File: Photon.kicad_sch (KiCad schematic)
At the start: 62 parts, among them J1 USB_C_Receptacle_USB2.0_14P, SW1 TS-1088-AR02016, U1 ATtiny13A-S, U2 RT8059GJ5, U3 BQ24072RGTR, U4 BCR421UW6-7, U5 BCR421UW6-7, U6 DW01A, U7 FS8205A, U8 TP4056

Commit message: added usb detection circuit and battery protection
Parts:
- removed C3, C4, C7: 4.7uF, Capacitor_SMD:C_0603_1608Metric, symbol Device:C
- removed D1, D2: SZYY0603R1, LED_SMD:LED_0603_1608Metric, symbol Device:LED
- removed R11, R7: 1.18K, Resistor_SMD:R_0603_1608Metric, symbol Device:R
- removed R21, R6, R8: 1K, Resistor_SMD:R_0603_1608Metric, symbol Device:R
- removed R5: 0R, Resistor_SMD:R_0603_1608Metric, symbol Device:R
- removed TP8: BuckEN, TestPoint:TestPoint_Pad_D1.0mm, symbol Connector:TestPoint
- removed TP9: BAT+, TestPoint:TestPoint_Pad_D1.0mm, symbol Connector:TestPoint
- removed U3: BQ24072RGTR, Photon:QFN-16_EP_3.8x3.8_Pitch0.5mm, symbol Photon:BQ24074RGTR
- added D8: D_Schottky, Diode_SMD:D_SOD-323F, symbol Device:D_Schottky
- added Q1: IRLML6402, Package_TO_SOT_SMD:SOT-23, symbol Transistor_FET:IRLML6402
- added R22: 100K, Resistor_SMD:R_0603_1608Metric, symbol Device:R
- added R23: 10K, Resistor_SMD:R_0603_1608Metric, symbol Device:R
- added TP10: BuckEN, TestPoint:TestPoint_Pad_D1.0mm, symbol Connector:TestPoint
- C10: Rating (none) -> XR5
- D3: Supplier https://jlcpcb.com/partdetail/YongyuPhotoelectric-SZYY0603R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 -> https://www.lcsc.com/datasheet/C19712529.pdf
- D6: Supplier https://jlcpcb.com/partdetail/YongyuPhotoelectric-SZYY0603R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 -> https://www.lcsc.com/datasheet/C19712529.pdfSZYY0603R1/C197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
- D7: Supplier https://jlcpcb.com/partdetail/YongyuPhotoelectric-SZYY0603R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 -> https://www.lcsc.com/datasheet/C19712529.pdf; Vf (none) -> 2V
- R10: value 100K -> 62K; Tolerance (none) -> 1%
- R13, R15, R3: value 10K -> 100K
- R18, R19: Tolerance (none) -> 1%
- R20: value 1K -> 2K
- R4: value 10K -> 0R
- R9: value 500K -> 280K; Tolerance (none) -> 1%
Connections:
- net 5V: now also R23.1
- net GND: now also R22.2; no longer R4.1
- net PACK+: now also Q1.3 (D); no longer U2.1 (EN)
- net LED_PWR: now reaches D6.2 (A)
- net LED_PWR: now also D7.2 (A), R20.2
- net STAT2: now reaches D7.1 (K), U8.6 (STAT2)
- net Iset: now reaches R19.1, U8.2 (ISET)
- net STAT1: now reaches D6.1 (K), U8.7 (STAT1)
- net VM: now reaches R18.2, U6.2 (VM)
- net BAT_SAF_OUT: now reaches C8.1, U6.6 (GND), U7.1 (S1)
- net BAT_SAF_OUT: now also D8.1 (K); no longer BT1.2 (-)
- net OC: now reaches U6.3 (OC), U7.4 (G2)
- net OD: now reaches U6.1 (OD), U7.6 (G1)
- net DW01A_VCC: now reaches C8.2, R17.2, U6.5 (VCC)
- net LED_A: now reaches D3.2 (A), R12.2
- net 3V6 renamed +3V3
- net TS renamed PMOS_OUT
- net PMOS_OUT: now also Q1.2 (S)
- new net: BT1.2 (-), D8.2 (A)
- new net BUCK_EN: R4.1, TP10.1, U2.1 (EN)
- new net PMOS_Gate: Q1.1 (G), R22.1, R23.2
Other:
- note added: "18650 Battery Vout=3.7V to 4.2V"
- note added: "Buck_FB = 0.6V Vo = 0.6 * (1+R1/R2) R2 = 60K to 300K"
- note added: "If usb present = disable buck"
- note added: "PACK Output = 3.39V to 3.89V"
- note added: "Vf = 0.31"
- note added: "Vf = 2V"
- note removed: "18650 Battery Vout=3.7-4.2V"
- note removed: "Vo = 0.6 * (1+R1/R2) R2 = 60K to 300K"
- moved on the sheet: C1, C2, C5, C6, D3, D4, D5, D6, D7, L1, R10, R12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

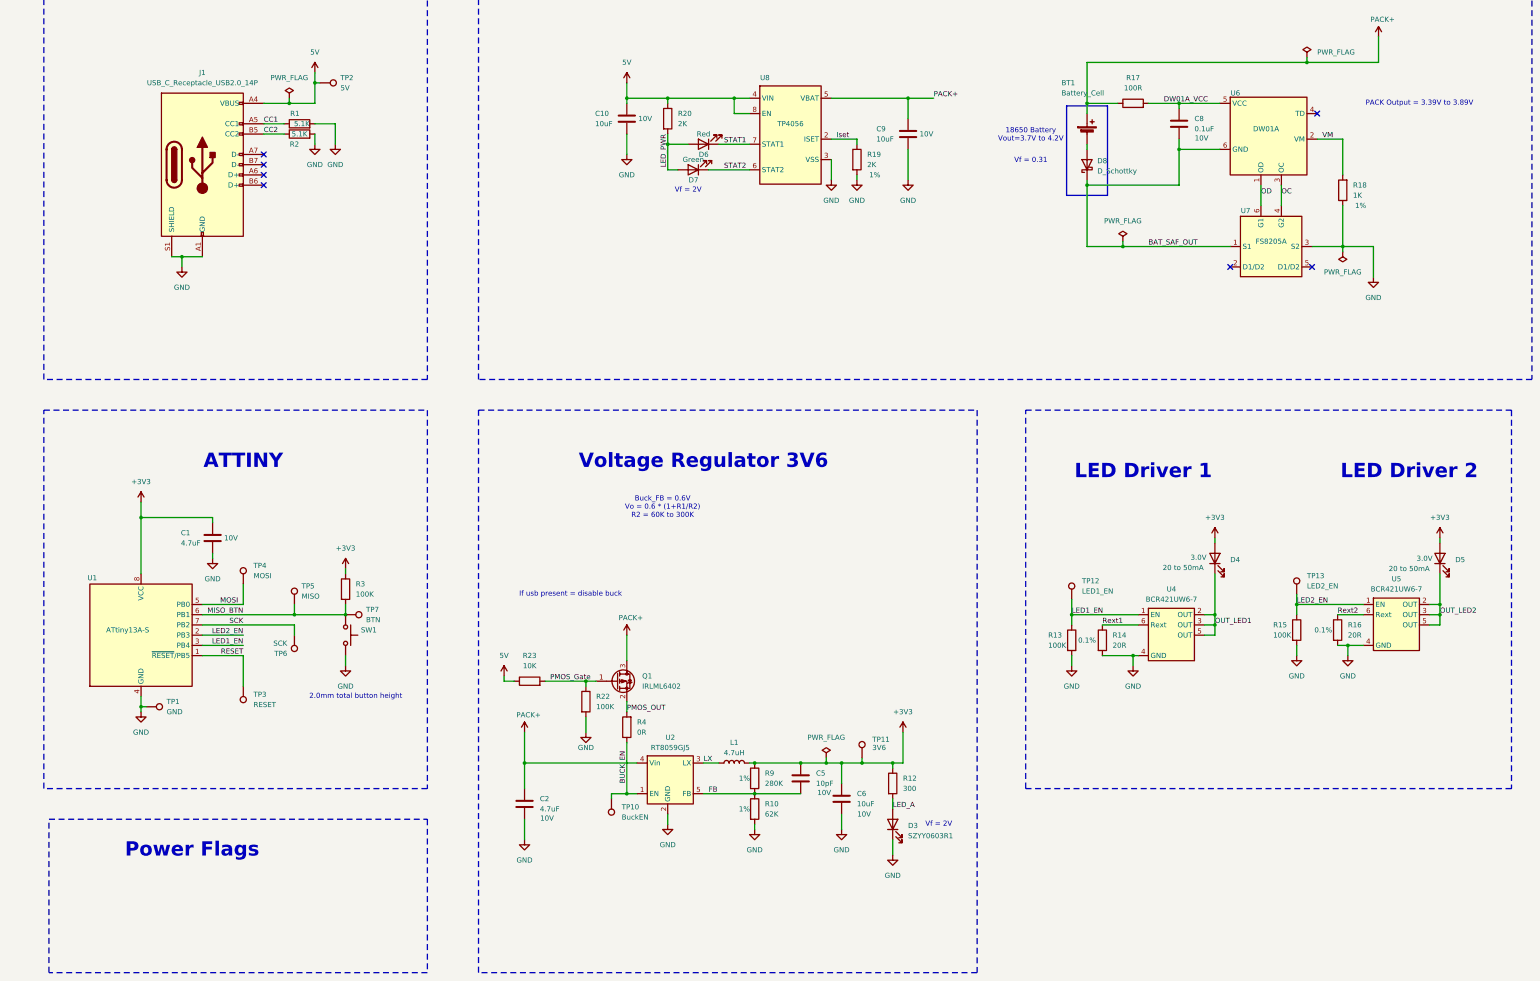
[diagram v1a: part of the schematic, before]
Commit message: PCB layout complete
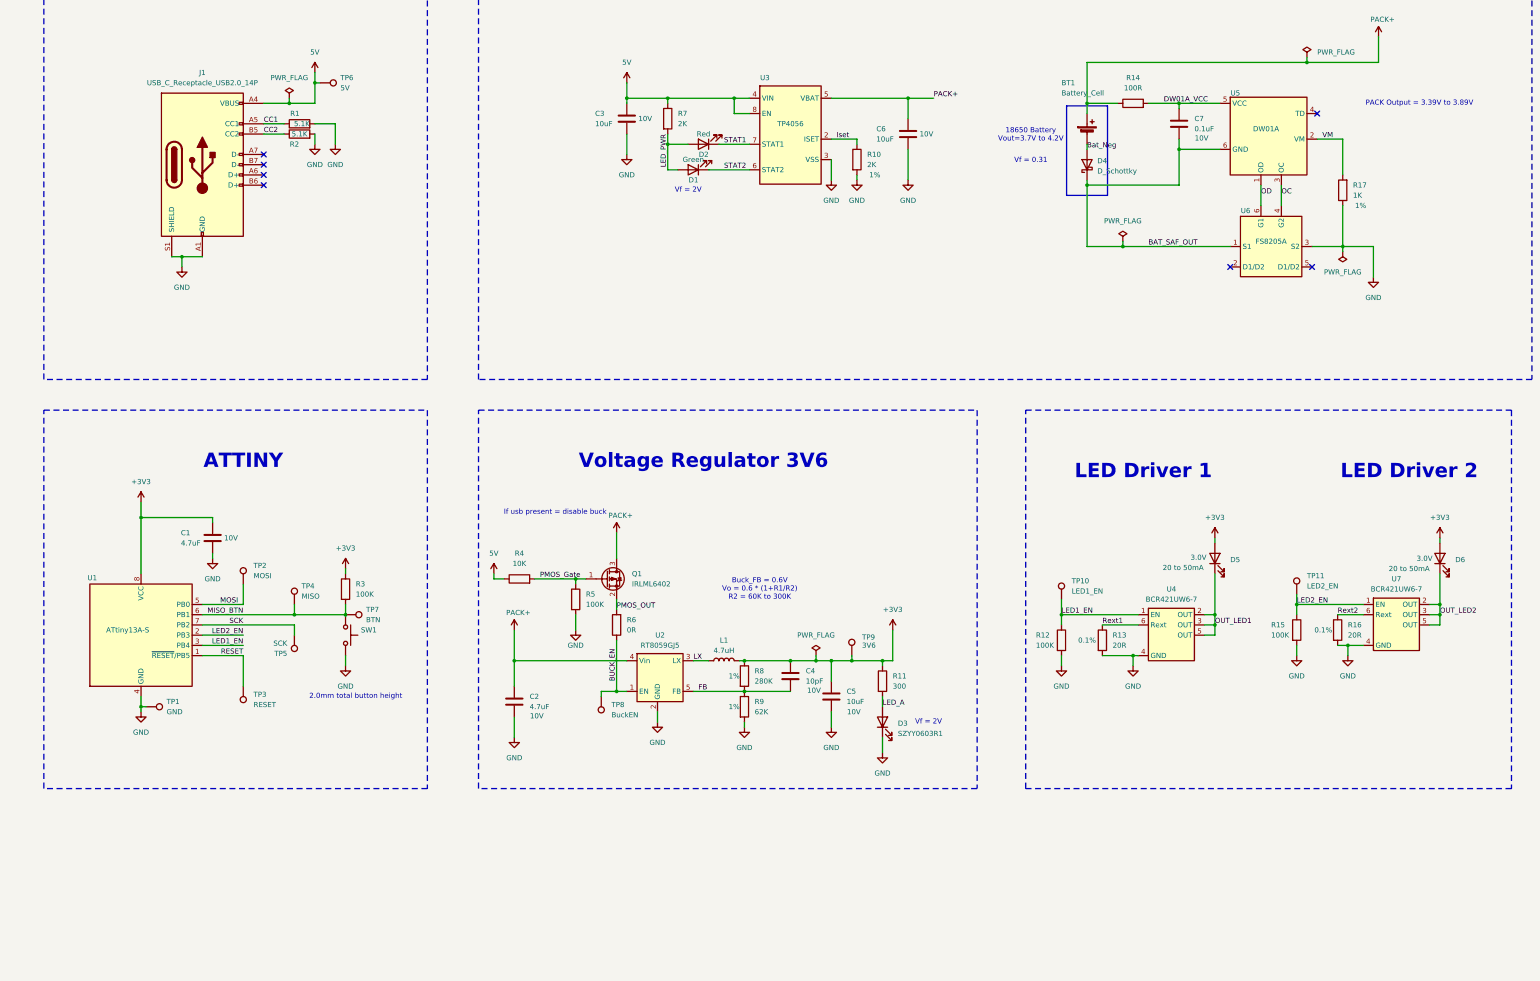
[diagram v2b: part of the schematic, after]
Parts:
- D4: renamed from D8; footprint Diode_SMD:D_SOD-323F -> Diode_SMD:D_SOD-323_HandSoldering
- U2: footprint Package_TO_SOT_SMD:SOT-23-5 -> Package_TO_SOT_SMD:SOT-23-5_HandSoldering
- U4: footprint Package_TO_SOT_SMD:SOT-23-6 -> Package_TO_SOT_SMD:SOT-23-6_Handsoldering
- U5: renamed from U6; footprint Package_TO_SOT_SMD:SOT-23-6 -> Package_TO_SOT_SMD:SOT-23-6_Handsoldering
- U6: renamed from U7; footprint Package_TO_SOT_SMD:SOT-23-6 -> Package_TO_SOT_SMD:SOT-23-6_Handsoldering
- U7: renamed from U5; footprint Package_TO_SOT_SMD:SOT-23-6 -> Package_TO_SOT_SMD:SOT-23-6_Handsoldering
- renumbered C10 to C3, C5 to C4, C6 to C5, C9 to C6, C8 to C7, D7 to D1, D6 to D2, D4 to D5, D5 to D6, R19 to R10, R12 to R11, R13 to R12, R14 to R13, R17 to R14, R18 to R17, R23 to R4, R22 to R5, R4 to R6, R20 to R7, R9 to R8, R10 to R9, TP12 to TP10, TP13 to TP11, TP4 to TP2, TP5 to TP4, TP6 to TP5, TP2 to TP6, TP10 to TP8, TP11 to TP9, U8 to U3
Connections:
- net Bat_Neg: now reaches BT1.2 (-), D4.2 (A)
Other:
- note removed: "Power Flags"
- moved on the sheet: C2, C4, C5, D3, L1, Q1, R11, R12, R4, R5, R6, R8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

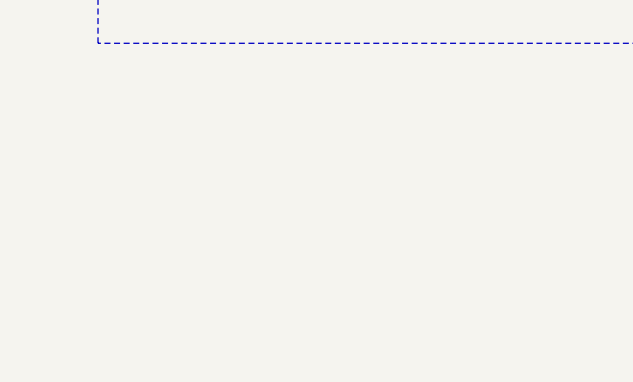
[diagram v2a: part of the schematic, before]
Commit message: added fiducials and gerbers. - Ordered
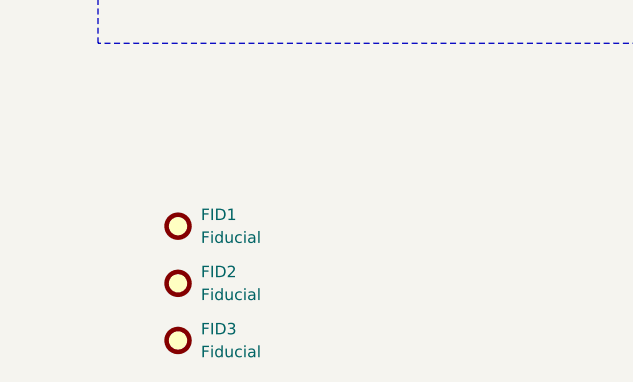
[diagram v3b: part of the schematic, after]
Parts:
- added FID1, FID2, FID3: Fiducial, Fiducial:Fiducial_0.5mm_Mask1.5mm, symbol Mechanical:Fiducial
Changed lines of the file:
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@@
 	)
 	(symbol
+		(lib_id "Mechanical:Fiducial")
+		(at 30.48 262.89 0)
+		(unit 1)
+		(exclude_from_sim no)
+		(in_bom no)
+		(on_board yes)
+		(dnp no)
+		(fields_autoplaced yes)
+		(property "Reference" "FID2"
+			(at 33.02 261.6199 0)
+			(effects
+				(font
+					(size 1.27 1.27)
+				)
+				(justify left)
+			)
+		)
+		(property "Value" "Fiducial"
+			(at 33.02 264.1599 0)
+			(effects
+				(font
+					(size 1.27 1.27)
+				)
+				(justify left)
+			)
+		)
+		(property "Footprint" "Fiducial:Fiducial_0.5mm_Mask1.5mm"
+			(at 30.48 262.89 0)
+			(effects
+				(font
+					(size 1.27 1.27)
+				)
+				(hide yes)
+			)
+		)
+		(property "Datasheet" "~"
+			(at 30.48 262.89 0)
+			(effects
+				(font
+					(size 1.27 1.27)
+				)
+				(hide yes)
+			)
+		)
+		(property "Description" "Fiducial Marker"
+			(at 30.48 262.89 0)
+			(effects
+				(font
+					(size 1.27 1.27)
+				)
+				(hide yes)
+			)
+		)
+		(instances
+			(project "Photon"
+				(path "/bca5ecdc-285a-4b7d-b583-3c5baee62e6e"
+					(reference "FID2")
+					(unit 1)
+				)
+			)
+		)
+	)
+	(symbol
 		(lib_id "power:GND")
 		(at 345.44 203.2 0)
@@
 	)
 	(symbol
+		(lib_id "Mechanical:Fiducial")
+		(at 30.48 256.54 0)
+		(unit 1)
+		(exclude_from_sim no)
+		(in_bom no)
+		(on_board yes)
+		(dnp no)
+		(fields_autoplaced yes)
+		(property "Reference" "FID1"
+			(at 33.02 255.2699 0)
+			(effects
+				(font
+					(size 1.27 1.27)
+				)
+				(justify left)
+			)
+		)
+		(property "Value" "Fiducial"
+			(at 33.02 257.8099 0)
+			(effects
+				(font
+					(size 1.27 1.27)
+				)
+				(justify left)
+			)
+		)
+		(property "Footprint" "Fiducial:Fiducial_0.5mm_Mask1.5mm"
+			(at 30.48 256.54 0)
+			(effects
+				(font
+					(size 1.27 1.27)
+				)
+				(hide yes)
+			)
+		)
+		(property "Datasheet" "~"
+			(at 30.48 256.54 0)
+			(effects
+				(font
+					(size 1.27 1.27)
+				)
+				(hide yes)
+			)
+		)
+		(property "Description" "Fiducial Marker"
+			(at 30.48 256.54 0)
+			(effects
+				(font
+					(size 1.27 1.27)
+				)
+				(hide yes)
+			)
+		)
+		(instances
+			(project ""
+				(path "/bca5ecdc-285a-4b7d-b583-3c5baee62e6e"
+					(reference "FID1")
+					(unit 1)
+				)
+			)
+		)
+	)
+	(symbol
 		(lib_id "Device:R")
 		(at 223.52 80.01 0)
@@
 					(unit 1)
 				)
+			)
+		)
+	)
+	(symbol
+		(lib_id "Mechanical:Fiducial")
+		(at 30.48 269.24 0)
+		(unit 1)
+		(exclude_from_sim no)
+		(in_bom no)
+		(on_board yes)
+		(dnp no)
+		(fields_autoplaced yes)
+		(property "Reference" "FID3"
+			(at 33.02 267.9699 0)
+			(effects
+				(font
+					(size 1.27 1.27)
+				)
+				(justify left)
+			)
+		)
+		(property "Value" "Fiducial"
+			(at 33.02 270.5099 0)
+			(effects
+				(font
+					(size 1.27 1.27)
+				)
+				(justify left)
+			)
+		)
+		(property "Footprint" "Fiducial:Fiducial_0.5mm_Mask1.5mm"
+			(at 30.48 269.24 0)
+			(effects
+				(font
+					(size 1.27 1.27)
+				)
+				(hide yes)
+			)
+		)
+		(property "Datasheet" "~"
+			(at 30.48 269.24 0)
+			(effects
+				(font
+					(size 1.27 1.27)
+				)
+				(hide yes)
+			)
+		)
+		(property "Description" "Fiducial Marker"
+			(at 30.48 269.24 0)
+			(effects
+				(font
+					(size 1.27 1.27)
+				)
+				(hide yes)
+			)
+		)
+		(instances
+			(project "Photon"
+				(path "/bca5ecdc-285a-4b7d-b583-3c5baee62e6e"
+					(reference "FID3")
+					(unit 1)
+				)

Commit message: updated gerbers
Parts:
- removed D4: D_Schottky, Diode_SMD:D_SOD-323_HandSoldering, symbol Device:D_Schottky
- added Q2: IRLML6402, Package_TO_SOT_SMD:SOT-23, symbol Transistor_FET:IRLML6402
- added R18: 10K, Resistor_SMD:R_0603_1608Metric, symbol Device:R
- added R19: 100K, Resistor_SMD:R_0603_1608Metric, symbol Device:R
- L1: value 4.7uH -> 2.2uH
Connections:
- net Bat_Neg is gone; now on net BAT_SAF_OUT: BT1.2 (-)
- net +3V3: now also R18.1
- net BAT_SAF_OUT: now also R19.2
- net PACK+: now also Q2.2 (S); no longer BT1.1 (+), R14.1
- net RESET: now also R18.2
- new net: Q2.1 (G), R19.1
- new net Bat+: BT1.1 (+), Q2.3 (D), R14.1
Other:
- note added: "PACK Output = 3.7V to 4.2V"
- note added: "Rds = 0.065R"
- note removed: "PACK Output = 3.39V to 3.89V"
- note removed: "Vf = 0.31"
- moved on the sheet: R3, SW1, TP3, TP4, TP5, TP7

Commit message: finished v3 of pcb
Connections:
- net BAT_DSBL: now reaches Q2.1 (G), R19.1
- net BAT_SAF_OUT renamed Bat-
- net PMOS_Gate renamed USB_DSBL
- net PMOS_OUT renamed PMOS_EN_OUT
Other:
- moved on the sheet: BT1
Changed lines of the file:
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@@
 	)
 	(rectangle
-		(start 275.59 66.675)
-		(end 285.75 88.9)
+		(start 275.59 64.77)
+		(end 285.75 80.01)
 		(stroke
 			(width 0)
@@
 	)
 	(junction
-		(at 280.67 86.36)
-		(diameter 0)
-		(color 0 0 0 0)
-	)
-	(junction
 		(at 345.44 200.66)
 		(diameter 0)
@@
 	)
 	(junction
+		(at 280.67 77.47)
+		(diameter 0)
+		(color 0 0 0 0)
+	)
+	(junction
 		(at 163.83 212.09)
 		(diameter 0)
@@
 	(wire
 		(pts
-			(xy 303.53 86.36) (xy 303.53 77.47)
+			(xy 193.04 68.58) (xy 193.04 64.77)
 		)
 		(stroke
@@
 	(wire
 		(pts
-			(xy 193.04 68.58) (xy 193.04 64.77)
+			(xy 280.67 77.47) (xy 280.67 101.6)
 		)
 		(stroke
@@
 	(wire
 		(pts
-			(xy 280.67 86.36) (xy 303.53 86.36)
+			(xy 280.67 77.47) (xy 303.53 77.47)
 		)
 		(stroke
@@
 	(wire
 		(pts
-			(xy 298.45 63.5) (xy 298.45 90.17)
-		)
-		(stroke
-			(width 0)
-			(type default)
-		)
-	)
-	(wire
-		(pts
 			(xy 76.2 66.04) (xy 82.55 66.04)
 		)
@@
 	(wire
 		(pts
-			(xy 280.67 66.04) (xy 280.67 68.58)
+			(xy 280.67 66.04) (xy 280.67 67.31)
 		)
 		(stroke
@@
 	(wire
 		(pts
-			(xy 280.67 76.2) (xy 280.67 86.36)
+			(xy 280.67 74.93) (xy 280.67 77.47)
 		)
 		(stroke
@@
 	(wire
 		(pts
-			(xy 328.93 86.36) (xy 328.93 91.44)
+			(xy 298.45 63.5) (xy 298.45 90.17)
 		)
 		(stroke
@@
 	(wire
 		(pts
-			(xy 163.83 212.09) (xy 166.37 212.09)
+			(xy 328.93 86.36) (xy 328.93 91.44)
 		)
 		(stroke
@@
 	(wire
 		(pts
-			(xy 342.9 193.04) (xy 349.25 193.04)
+			(xy 163.83 212.09) (xy 166.37 212.09)
 		)
 		(stroke
@@
 	(wire
 		(pts
-			(xy 45.72 168.91) (xy 45.72 182.88)
+			(xy 342.9 193.04) (xy 349.25 193.04)
 		)
 		(stroke
@@
 	(wire
 		(pts
-			(xy 368.3 193.04) (xy 365.76 193.04)
+			(xy 45.72 168.91) (xy 45.72 182.88)
 		)
 		(stroke
@@
 	(wire
 		(pts
-			(xy 280.67 86.36) (xy 280.67 101.6)
+			(xy 368.3 193.04) (xy 365.76 193.04)
 		)
 		(stroke
@@
 		)
 	)
+	(label "BAT_DSBL"
+		(at 298.45 83.82 0)
+		(effects
+			(font
+				(size 1.27 1.27)
+			)
+			(justify left bottom)
+		)
+	)
 	(label "LED_PWR"
 		(at 176.53 73.66 270)
@@
 		)
 	)
-	(label "Bat_Neg"
-		(at 280.67 77.47 0)
+	(label "Bat-"
+		(at 280.67 85.09 0)
 		(effects
 			(font
@@
 		)
 	)
-	(label "BAT_SAF_OUT"
-		(at 300.99 101.6 0)
-		(effects
-			(font
-				(size 1.27 1.27)
-			)
-			(justify left bottom)
-		)
-	)
 	(label "CC2"
 		(at 76.2 73.66 0)
@@
 		)
 	)
-	(label "PMOS_OUT"
+	(label "PMOS_EN_OUT"
 		(at 163.83 191.77 0)
 		(effects
@@
 		)
 	)
-	(label "PMOS_Gate"
+	(label "USB_DSBL"
 		(at 144.78 184.15 0)
 		(effects
@@
 	(symbol
 		(lib_id "Device:Battery_Cell")
-		(at 280.67 73.66 0)
+		(at 280.67 72.39 0)
 		(unit 1)
 		(exclude_from_sim no)
@@
 		(dnp no)
 		(property "Reference" "BT1"
-			(at 274.32 60.96 0)
+			(at 274.32 59.69 0)
 			(effects
 				(font
@@
 		)
 		(property "Value" "Battery_Cell"
-			(at 274.32 63.5 0)
+			(at 274.32 62.23 0)
 			(effects
 				(font
@@
 		)
 		(property "Footprint" "Photon:18650 Battery Holder"
-			(at 280.67 72.136 90)
+			(at 280.67 70.866 90)
 			(effects
 				(font
@@
 		)
 		(property "Datasheet" "~"
-			(at 280.67 72.136 90)
+			(at 280.67 70.866 90)
 			(effects
 				(font
@@
 		)
 		(property "Description" "Single-cell battery"
-			(at 280.67 73.66 0)
+			(at 280.67 72.39 0)
 			(effects
 				(font

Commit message: v1.3
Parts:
- TP9: value 3V6 -> 3V3
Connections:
- net BAT_DSBL: now also R19.2; no longer R19.1
- net Bat+: now also C6.2, U3.5 (VBAT)
- net Bat-: now also R19.1; no longer R19.2
- net PACK+ renamed PACK_Safe
- net PACK_Safe: no longer C6.2, U3.5 (VBAT)
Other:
- moved on the sheet: BT1, C3, C6, C7, D1, D2, Q2, R10, R14, R17, R19, R7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

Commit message: Cleaned up PCB
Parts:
- removed D3: SZYY0603R1, LED_SMD:LED_0603_1608Metric, symbol Device:LED
- removed R11: 300, Resistor_SMD:R_0603_1608Metric, symbol Device:R
- removed R3: 100K, Resistor_SMD:R_0603_1608Metric, symbol Device:R
- removed TP2: MOSI, TestPoint:TestPoint_Pad_D1.0mm, symbol Connector:TestPoint
- removed TP3: RESET, TestPoint:TestPoint_Pad_D1.0mm, symbol Connector:TestPoint
- removed TP4: MISO, TestPoint:TestPoint_Pad_D1.0mm, symbol Connector:TestPoint
- removed TP5: SCK, TestPoint:TestPoint_Pad_D1.0mm, symbol Connector:TestPoint
- added TP12: SCK, TestPoint:TestPoint_Pad_D1.0mm, symbol Connector:TestPoint
- added TP13: RESET, TestPoint:TestPoint_Pad_D1.0mm, symbol Connector:TestPoint
- added TP14: 3V3, TestPoint:TestPoint_THTPad_D1.0mm_Drill0.5mm, symbol Connector:TestPoint
- added TP15: GND, TestPoint:TestPoint_Pad_D1.0mm, symbol Connector:TestPoint
- BT1: footprint Photon:18650 Battery Holder -> Photon:Spring Battery TH
- R4: value 10K -> 100R
- R6: value 0R -> 100K
- TP10, TP11, TP6: footprint TestPoint:TestPoint_Pad_D1.0mm -> TestPoint:TestPoint_THTPad_D1.0mm_Drill0.5mm; now not fitted
- TP7: value BTN -> MOSI
- TP8: value BuckEN -> MISO
- U4, U5, U6, U7: footprint Package_TO_SOT_SMD:SOT-23-6_Handsoldering -> Package_TO_SOT_SMD:SOT-23-6
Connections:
- net +3V3: now also TP14.1
- net 5V: now also R4.2, R5.1; no longer R4.1
- net BUCK_EN: now also Q1.3 (D); no longer TP8.1
- net GND: now also R6.2, TP15.1
- net MISO_BTN: now also TP8.1; no longer TP7.1
- net MOSI: now also TP7.1
- net RESET: now also TP13.1
- net SCK: now also TP12.1
- net PACK_Safe renamed PACK_SAFE
- net PACK_SAFE: now also Q1.2 (S); no longer Q1.3 (D)
- removed net PMOS_EN_OUT: Q1.2 (S), R6.2
- removed net USB_DSBL: Q1.1 (G), R4.2, R5.1
- new net DSBL: Q1.1 (G), R4.1
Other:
- note added: "If usb present -> disable buck"
- note added: "PACK_SAFE Output = 3.7V to 4.2V"
- note removed: "If usb present = disable buck"
- note removed: "PACK Output = 3.7V to 4.2V"
- moved on the sheet: C1, C2, C3, C4, C5, FID1, FID2, FID3, L1, Q1, R12, R15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
